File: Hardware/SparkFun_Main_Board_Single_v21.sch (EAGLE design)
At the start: 84 parts, among them J1 MICROMOD-2222-C, J10 MICRO-SD-PUSH-PUSH-EXT-PIN, J2 Vertical Qwiic Connector, J4 QWIIC_RIGHT_ANGLE, J5 CORTEX_JTAG_DEBUG_MINIMUM_PTH, J6 MICROMOD_FUNCTION_MAIN, Q1 3.1A/30V/105mΩ, Q2 20V/4.2A/52mΩ/1.4W, U1 STG3856QTR, U2 MCP73831, U3 ESD Diode, U4 AP7347DQ-33W5-7K-3.3V, U5 AP7361C-33

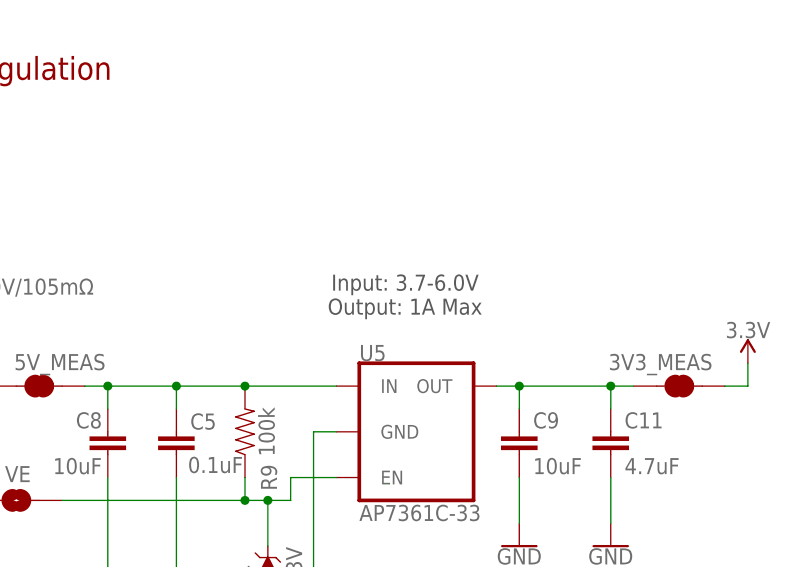
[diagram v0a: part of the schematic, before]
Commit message: Updat input voltage range on the VREG
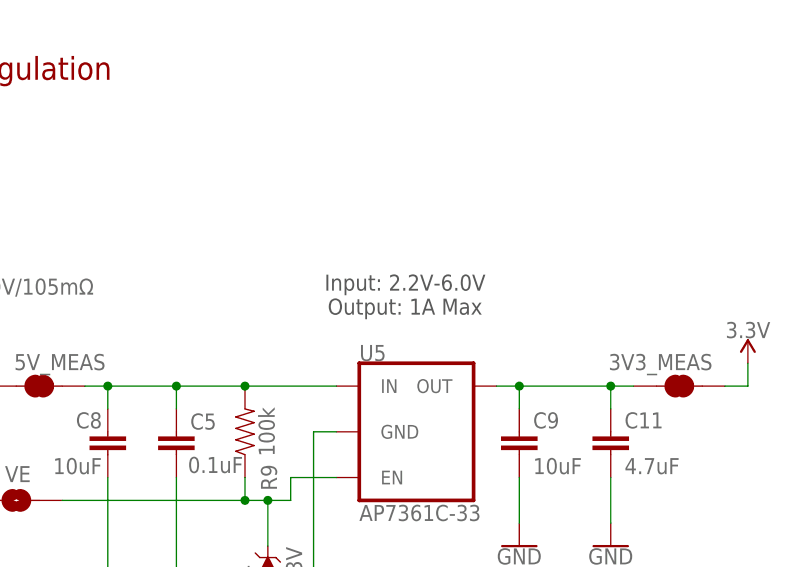
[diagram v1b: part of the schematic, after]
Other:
- note added: "Input: 2.2V-6.0V Output: 1A Max"
- note removed: "Input: 3.7-6.0V Output: 1A Max"
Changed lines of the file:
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@@
 <?xml version="1.0" encoding="utf-8"?>
 <!DOCTYPE eagle SYSTEM "eagle.dtd">
-<eagle version="9.6.2">
+<eagle version="9.4.2">
 <drawing>
 <settings>
@@
 <text x="233.68" y="263.652" size="1.778" layer="97" font="vector" align="center">Closing jumper bypasses PTC
 to allow &gt;2A current flows.</text>
-<text x="360.68" y="246.38" size="1.778" layer="97" font="vector" align="center">Input: 3.7-6.0V
+<text x="360.68" y="246.38" size="1.778" layer="97" font="vector" align="center">Input: 2.2V-6.0V
 Output: 1A Max</text>
 <text x="284.48" y="210.82" size="1.778" layer="97" font="vector" align="center">Close VE to enable processor

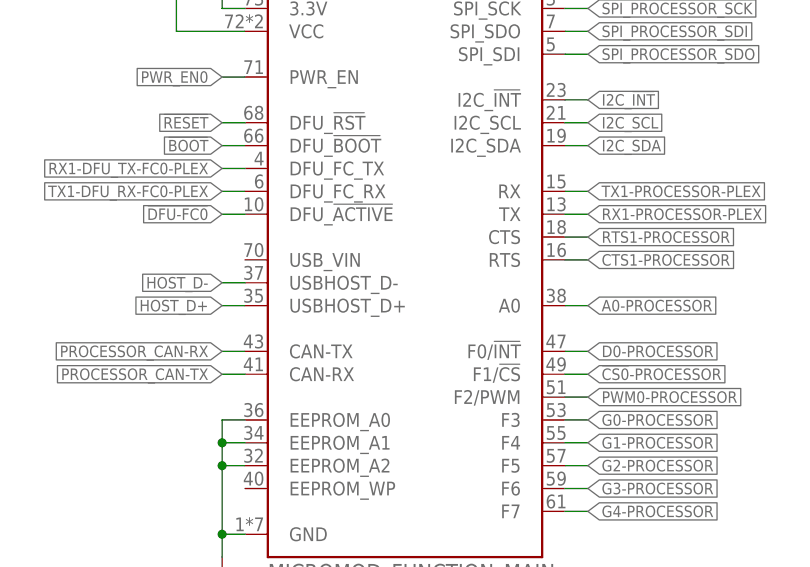
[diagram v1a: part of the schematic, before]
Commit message: Updates function board symbol
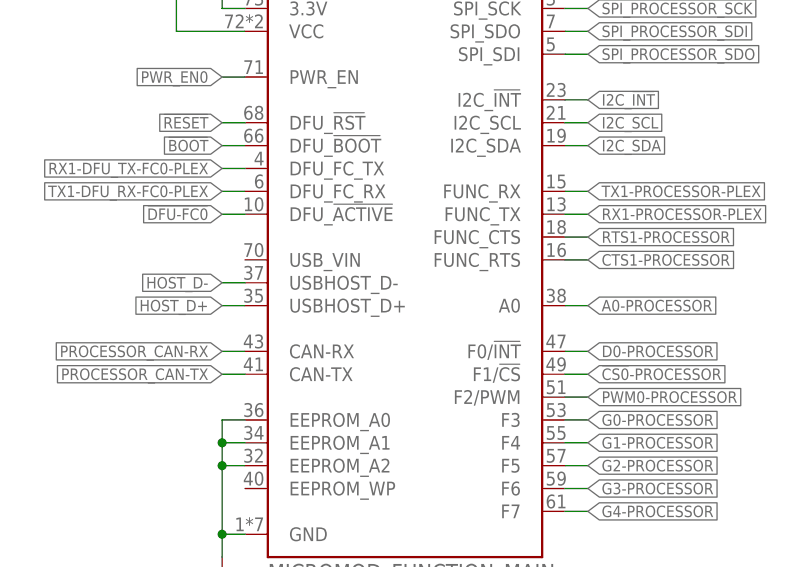
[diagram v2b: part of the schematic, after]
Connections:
- net CTS1-PROCESSOR: now also J6.FUNC_RTS; no longer J6.RTS
- net PROCESSOR_CAN-RX: now also J6.CAN-RX; no longer J6.CAN-TX
- net PROCESSOR_CAN-TX: now also J6.CAN-TX; no longer J6.CAN-RX
- net RTS1-PROCESSOR: now also J6.FUNC_CTS; no longer J6.CTS
- net RX1-PROCESSOR-PLEX: now also J6.FUNC_TX; no longer J6.TX
- net TX1-PROCESSOR-PLEX: now also J6.FUNC_RX; no longer J6.RX
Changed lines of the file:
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@@
 <wire x1="76.2" y1="60.96" x2="73.66" y2="60.96" width="0.1524" layer="91"/>
 <label x="73.66" y="60.96" size="1.27" layer="95" font="vector" rot="R180" xref="yes"/>
-<pinref part="J6" gate="J1" pin="CAN-RX"/>
+<pinref part="J6" gate="J1" pin="CAN-TX"/>
 </segment>
 </net>
@@
 <wire x1="76.2" y1="63.5" x2="73.66" y2="63.5" width="0.1524" layer="91"/>
 <label x="73.66" y="63.5" size="1.27" layer="95" font="vector" rot="R180" xref="yes"/>
-<pinref part="J6" gate="J1" pin="CAN-TX"/>
+<pinref part="J6" gate="J1" pin="CAN-RX"/>
 </segment>
 <segment>
@@
 <wire x1="111.76" y1="73.66" x2="114.3" y2="73.66" width="0.1524" layer="91"/>
 <label x="114.3" y="73.66" size="1.27" layer="95" font="vector" xref="yes"/>
-<pinref part="J6" gate="J1" pin="RTS"/>
+<pinref part="J6" gate="J1" pin="FUNC_RTS"/>
 </segment>
 </net>
@@
 <wire x1="111.76" y1="76.2" x2="114.3" y2="76.2" width="0.1524" layer="91"/>
 <label x="114.3" y="76.2" size="1.27" layer="95" font="vector" xref="yes"/>
-<pinref part="J6" gate="J1" pin="CTS"/>
+<pinref part="J6" gate="J1" pin="FUNC_CTS"/>
 </segment>
 </net>
@@
 <wire x1="111.76" y1="81.28" x2="114.3" y2="81.28" width="0.1524" layer="91"/>
 <label x="114.3" y="81.28" size="1.27" layer="95" font="vector" xref="yes"/>
-<pinref part="J6" gate="J1" pin="RX"/>
+<pinref part="J6" gate="J1" pin="FUNC_RX"/>
 </segment>
 <segment>
@@
 <wire x1="111.76" y1="78.74" x2="114.3" y2="78.74" width="0.1524" layer="91"/>
 <label x="114.3" y="78.74" size="1.27" layer="95" font="vector" xref="yes"/>
-<pinref part="J6" gate="J1" pin="TX"/>
-</segment>
-<segment>
+<pinref part="J6" gate="J1" pin="FUNC_TX"/>
+</segment>
+<segment>
